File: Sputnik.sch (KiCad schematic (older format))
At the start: 0 parts

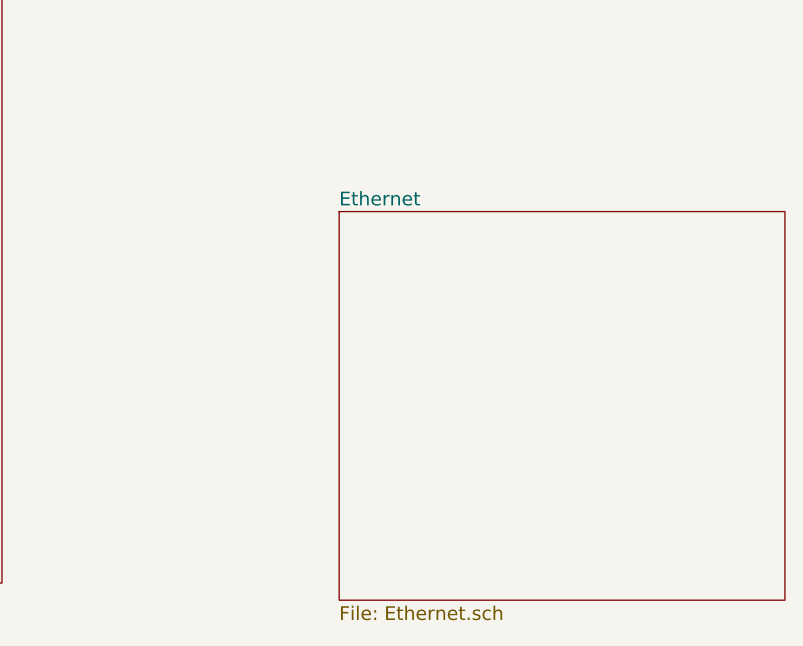
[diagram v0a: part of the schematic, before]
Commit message: Pulse jack added
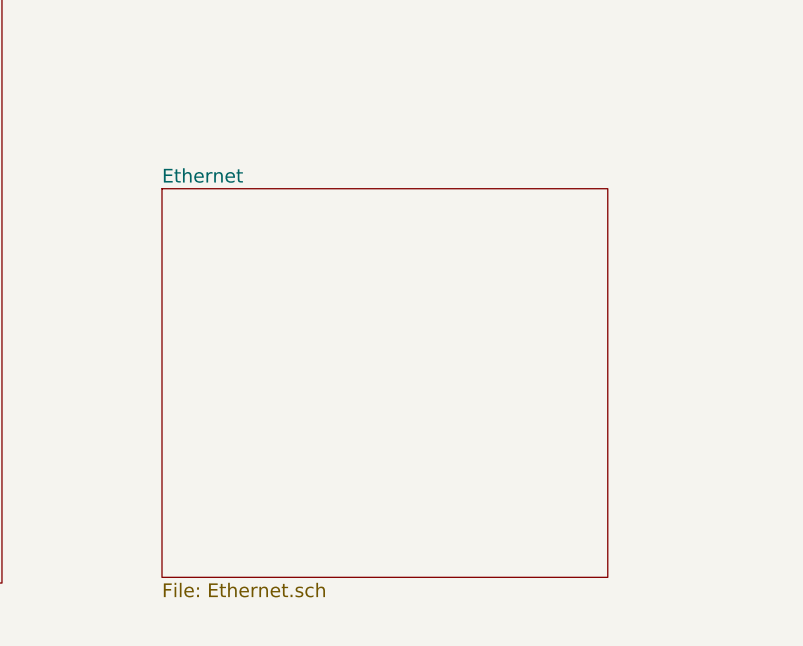
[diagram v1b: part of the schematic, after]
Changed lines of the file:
@@
 	4600 4725 3100 4725
 $Sheet
-S 12075 4350 1950 1700
+S 11300 4250 1950 1700
 U 57F77ED3
 F0 "Ethernet" 60

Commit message: Update
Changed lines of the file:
@@
 F33 "E_CLOCK_" I L 4600 3700 60
 F34 "nSLAVEn_IN" I L 4600 3375 60
+F35 "nRESET" O L 4600 4950 60
+F36 "CMD" O R 10600 4800 60
+F37 "INT" I R 10600 4950 60
+F38 "IOR#" O R 10600 5025 60
+F39 "IOW#" O R 10600 5100 60
+F40 "CS#" O R 10600 5175 60
+F41 "IORST#" O R 10600 5250 60
+F42 "ETH_SD[0:15]" B R 10600 4350 60
 $EndSheet
 Wire Bus Line
@@
 F0 "Ethernet" 60
 F1 "Ethernet.sch" 60
+F2 "ETH_SD[0:15]" B L 11300 4350 60
+F3 "CMD" I L 11300 4800 60
+F4 "INT" O L 11300 4950 60
+F5 "IOR#" I L 11300 5025 60
+F6 "IOW#" I L 11300 5100 60
+F7 "CS#" I L 11300 5175 60
+F8 "PWRST#" I L 11300 5250 60
 $EndSheet
 Wire Wire Line
@@
 Wire Wire Line
 	3100 3375 4600 3375
+Wire Wire Line
+	10600 4800 11300 4800
+Wire Wire Line
+	11300 4950 10600 4950
+Wire Wire Line
+	10600 5025 11300 5025
+Wire Wire Line
+	11300 5100 10600 5100
+Wire Wire Line
+	10600 5175 11300 5175
+Wire Wire Line
+	10600 5250 11300 5250
+Wire Bus Line
+	10600 4350 11300 4350
 $EndSCHEMATC

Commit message: More routing
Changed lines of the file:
@@
 F20 "SenseZ3" I L 4600 3225 60
 F21 "nSLAVEn" O L 4600 3300 60
-F22 "nDTACK" B L 4600 3925 60
+F22 "nDTACK" I L 4600 3925 60
 F23 "nHLT" B L 4600 4000 60
 F24 "nCINH" B L 4600 4225 60
@@
 F41 "IORST#" O R 10600 5250 60
 F42 "ETH_SD[0:15]" B R 10600 4350 60
+F43 "nDTACK_OUT" O L 4600 3850 60
 $EndSheet
 Wire Bus Line
@@
 F5 "nCINH" B R 3100 4225 60
 F6 "nBERR" B R 3100 4375 60
-F7 "nDTACK" B R 3100 3925 60
-F8 "nINT2" I R 3100 4300 60
-F9 "nINT6" I R 3100 4450 60
-F10 "nLOCK" B R 3100 1075 60
-F11 "nDS_[0..3]" B R 3100 1950 60
-F12 "nFCS" B R 3100 1150 60
-F13 "nCCS" B R 3100 1225 60
-F14 "nIORST" B R 3100 2225 60
-F15 "nBCLR" B R 3100 2300 60
-F16 "DOE_" B R 3100 1300 60
-F17 "READ_" B R 3100 1375 60
-F18 "nMTACK" B R 3100 2375 60
-F19 "nMTCR" B R 3100 2450 60
-F20 "A_[2..7]" B R 3100 2050 60
-F21 "nHLT" B R 3100 4000 60
-F22 "nCFGINn" O R 3100 2925 60
-F23 "nCFGOUTn" I R 3100 3000 60
-F24 "nBRn" I R 3100 3075 60
-F25 "nBGn" O R 3100 3150 60
-F26 "DIR_AD" I R 3100 4650 60
-F27 "nOE_AD" I R 3100 4725 60
-F28 "SenseZ3_" O R 3100 3225 60
-F29 "BUSMASTER" I R 3100 5350 60
-F30 "7M_" O R 3100 3475 60
-F31 "E_CLOCK_" O R 3100 3700 60
-F32 "nBGACK" B R 3100 2525 60
-F33 "nOWN" B R 3100 2600 60
-F34 "nSLAVEn_OUT" I R 3100 3300 60
-F35 "nSLAVEn_IN" O R 3100 3375 60
+F7 "nINT2" I R 3100 4300 60
+F8 "nINT6" I R 3100 4450 60
+F9 "nLOCK" B R 3100 1075 60
+F10 "nDS_[0..3]" B R 3100 1950 60
+F11 "nFCS" B R 3100 1150 60
+F12 "nCCS" B R 3100 1225 60
+F13 "nIORST" B R 3100 2225 60
+F14 "nBCLR" B R 3100 2300 60
+F15 "DOE_" B R 3100 1300 60
+F16 "READ_" B R 3100 1375 60
+F17 "nMTACK" B R 3100 2375 60
+F18 "nMTCR" B R 3100 2450 60
+F19 "A_[2..7]" B R 3100 2050 60
+F20 "nHLT" B R 3100 4000 60
+F21 "nCFGINn" O R 3100 2925 60
+F22 "nCFGOUTn" I R 3100 3000 60
+F23 "nBRn" I R 3100 3075 60
+F24 "nBGn" O R 3100 3150 60
+F25 "DIR_AD" I R 3100 4650 60
+F26 "nOE_AD" I R 3100 4725 60
+F27 "SenseZ3_" O R 3100 3225 60
+F28 "BUSMASTER" I R 3100 5350 60
+F29 "7M_" O R 3100 3475 60
+F30 "E_CLOCK_" O R 3100 3700 60
+F31 "nBGACK" B R 3100 2525 60
+F32 "nOWN" B R 3100 2600 60
+F33 "nSLAVEn_OUT" I R 3100 3300 60
+F34 "nSLAVEn_IN" O R 3100 3375 60
+F35 "nBUSMASTER" I R 3100 5450 60
+F36 "nDTACK_OUT" I R 3100 3850 60
+F37 "nDTACK" O R 3100 3925 60
 $EndSheet
 Wire Wire Line
@@
 Wire Bus Line
 	10600 4350 11300 4350
+Wire Wire Line
+	3100 3850 4600 3850
 $EndSCHEMATC

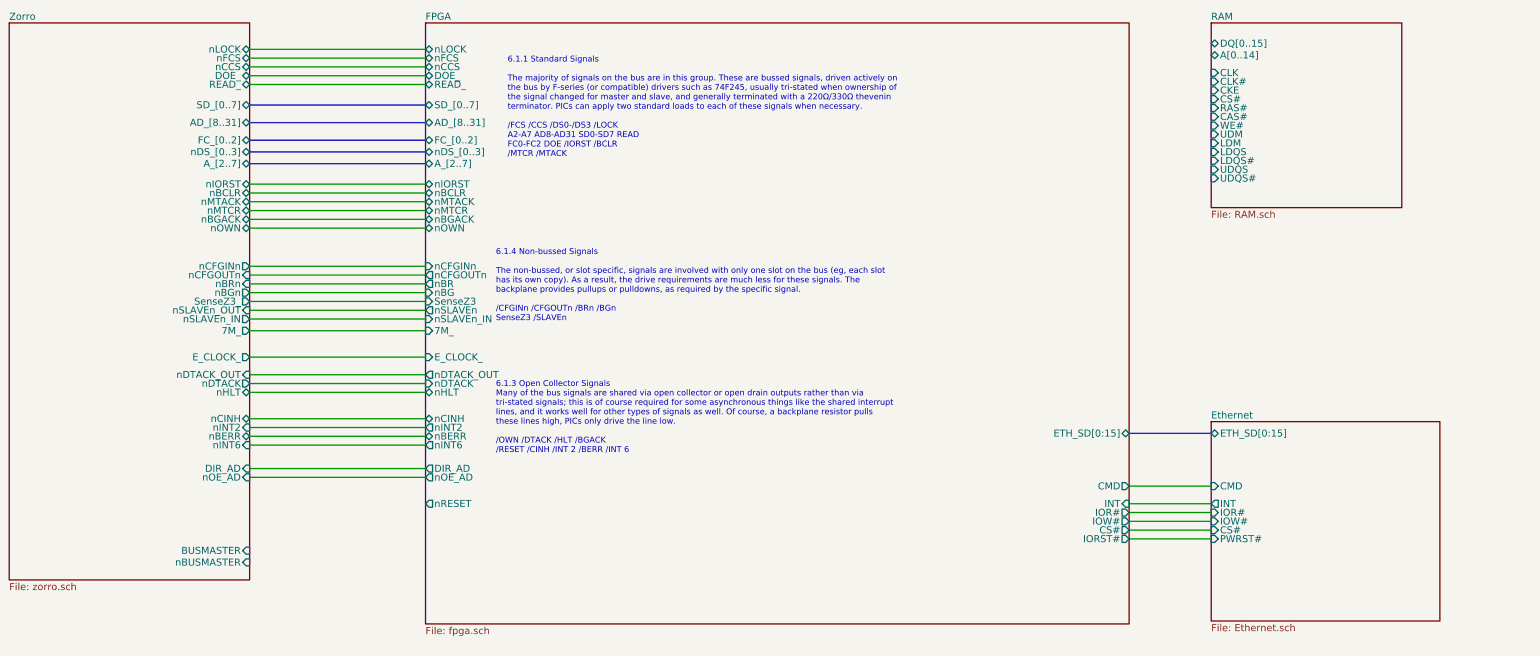
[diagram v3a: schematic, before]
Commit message: Inner layers routing
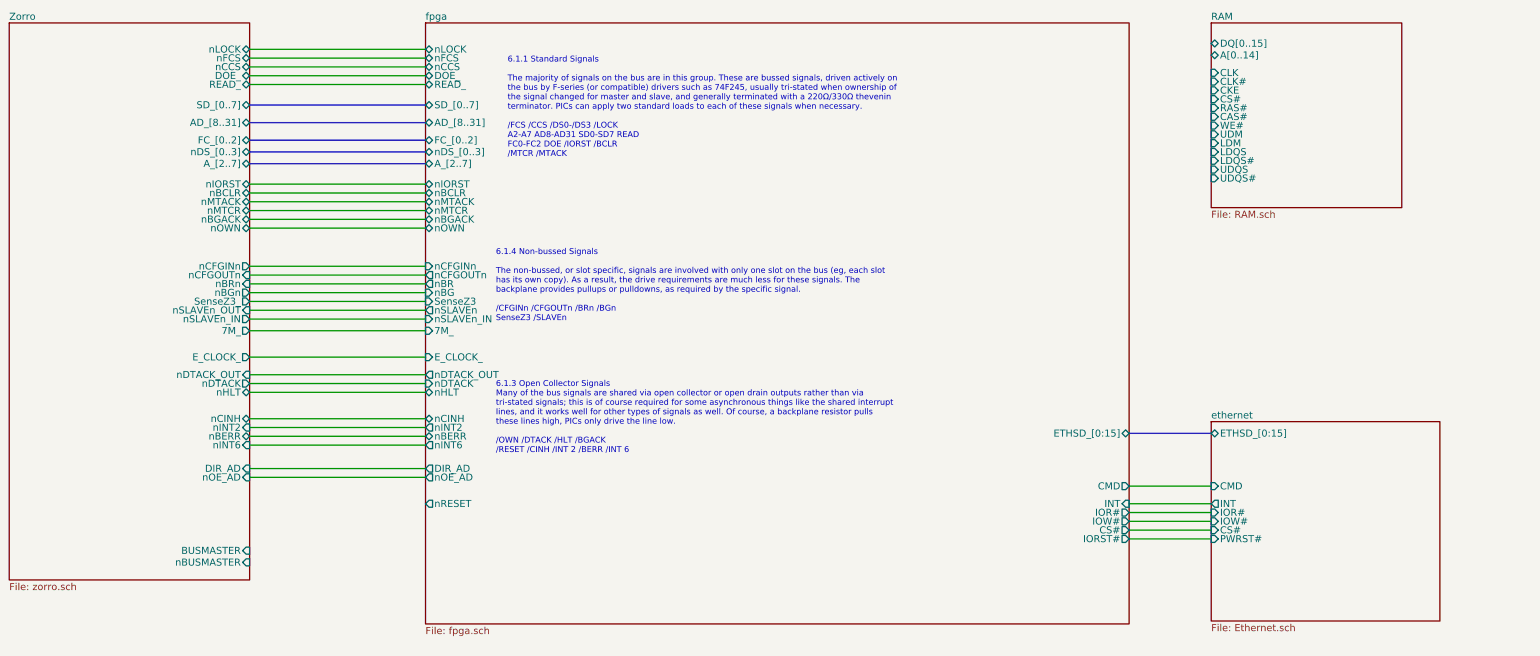
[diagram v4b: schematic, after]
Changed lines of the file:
@@
 S 4600 850  6000 5125
 U 58078329
-F0 "FPGA" 60
+F0 "fpga" 60
 F1 "fpga.sch" 60
 F2 "SD_[0..7]" B L 4600 1550 60
@@
 F40 "CS#" O R 10600 5175 60
 F41 "IORST#" O R 10600 5250 60
-F42 "ETH_SD[0:15]" B R 10600 4350 60
-F43 "nDTACK_OUT" O L 4600 3850 60
+F42 "nDTACK_OUT" O L 4600 3850 60
+F43 "ETHSD_[0:15]" B R 10600 4350 60
 $EndSheet
 Wire Bus Line
@@
 S 11300 4250 1950 1700
 U 57F77ED3
-F0 "Ethernet" 60
+F0 "ethernet" 60
 F1 "Ethernet.sch" 60
-F2 "ETH_SD[0:15]" B L 11300 4350 60
-F3 "CMD" I L 11300 4800 60
-F4 "INT" O L 11300 4950 60
-F5 "IOR#" I L 11300 5025 60
-F6 "IOW#" I L 11300 5100 60
-F7 "CS#" I L 11300 5175 60
-F8 "PWRST#" I L 11300 5250 60
+F2 "CMD" I L 11300 4800 60
+F3 "INT" O L 11300 4950 60
+F4 "IOR#" I L 11300 5025 60
+F5 "IOW#" I L 11300 5100 60
+F6 "CS#" I L 11300 5175 60
+F7 "PWRST#" I L 11300 5250 60
+F8 "ETHSD_[0:15]" B L 11300 4350 60
 $EndSheet
 Wire Wire Line
@@
 Wire Wire Line
 	10600 5250 11300 5250
+Wire Wire Line
+	3100 3850 4600 3850
 Wire Bus Line
 	10600 4350 11300 4350
-Wire Wire Line
-	3100 3850 4600 3850
 $EndSCHEMATC

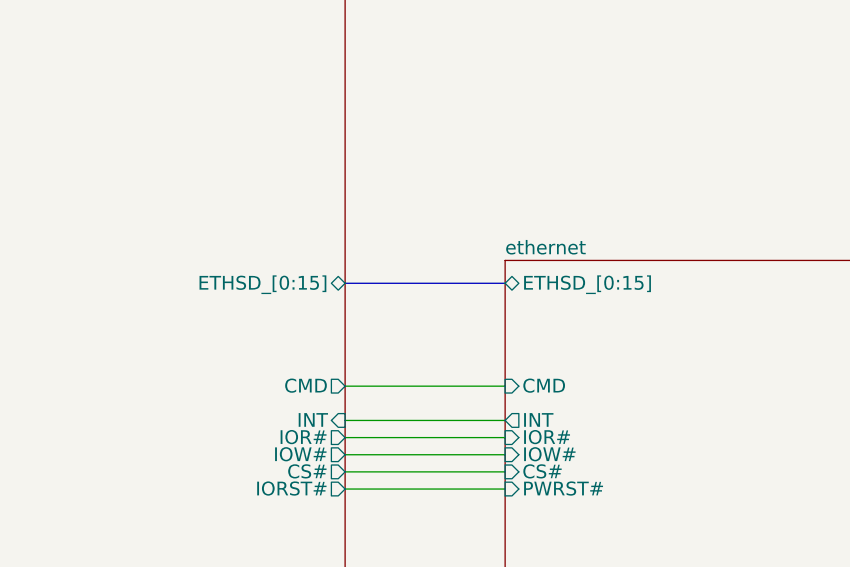
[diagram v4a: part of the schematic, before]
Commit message: Ethernet SD bus resolved
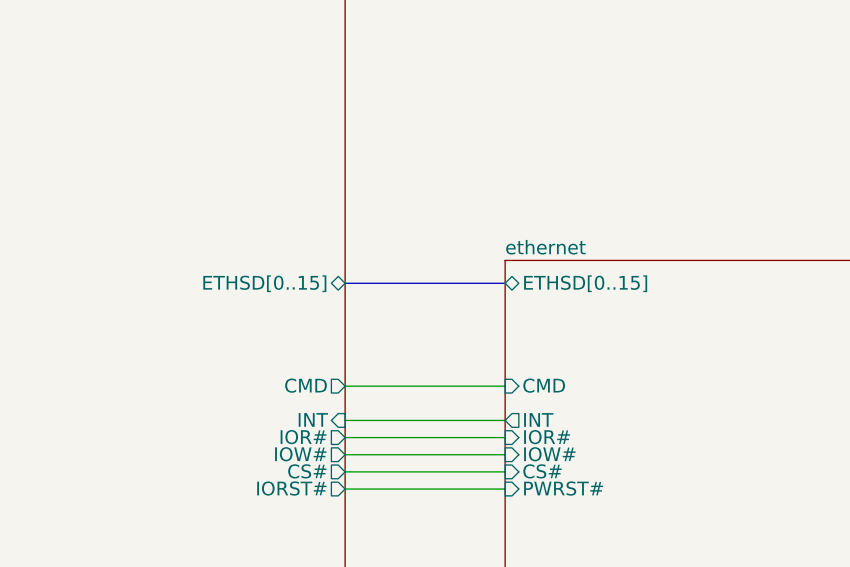
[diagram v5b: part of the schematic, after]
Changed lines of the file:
@@
 F41 "IORST#" O R 10600 5250 60
 F42 "nDTACK_OUT" O L 4600 3850 60
-F43 "ETHSD_[0:15]" B R 10600 4350 60
+F43 "ETHSD[0..15]" B R 10600 4350 60
 $EndSheet
 Wire Bus Line
@@
 F6 "CS#" I L 11300 5175 60
 F7 "PWRST#" I L 11300 5250 60
-F8 "ETHSD_[0:15]" B L 11300 4350 60
+F8 "ETHSD[0..15]" B L 11300 4350 60
 $EndSheet
 Wire Wire Line
